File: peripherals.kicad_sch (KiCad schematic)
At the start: 93 parts, among them J10 533980471, J11 ERF8-040-05.0-L-DV-K-TR, J14 SM04B-SRSS-TB-LF-SN, J9 TC2050-IDC-NL, Q10 PJE138K, Q9 PJE138K, U30 TPD4E05U06QDQARQ1, U33 NTS0102GT, U34 PCAL6408ABSHP, U35 AP22653FDZ-7

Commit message: Renaming Sheets
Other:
- company: Antmicro Ltd -> Dronolab
- title: Jetson Orin Baseboard -> Peripherals
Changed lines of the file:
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@@
   (paper "A3")
   (title_block
-    (title "Jetson Orin Baseboard")
-    (date "2023-03-03")
-    (rev "1.1.0")
-    (company "Antmicro Ltd")
-    (comment 1 "www.antmicro.com")
+    (title "Peripherals")
+    (date "2023-07-05")
+    (rev "1.0.0")
+    (company "Dronolab")
+    (comment 1 "dronolab.etsmtl.ca")
   )
   (junction (at 248.285 253.365) (diameter 0) (color 0 0 0 0)

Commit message: Simplification continues
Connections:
- net DISABLE_POE_DCDC: no longer names the net of R25.4
- no-connect marks 12 -> 13

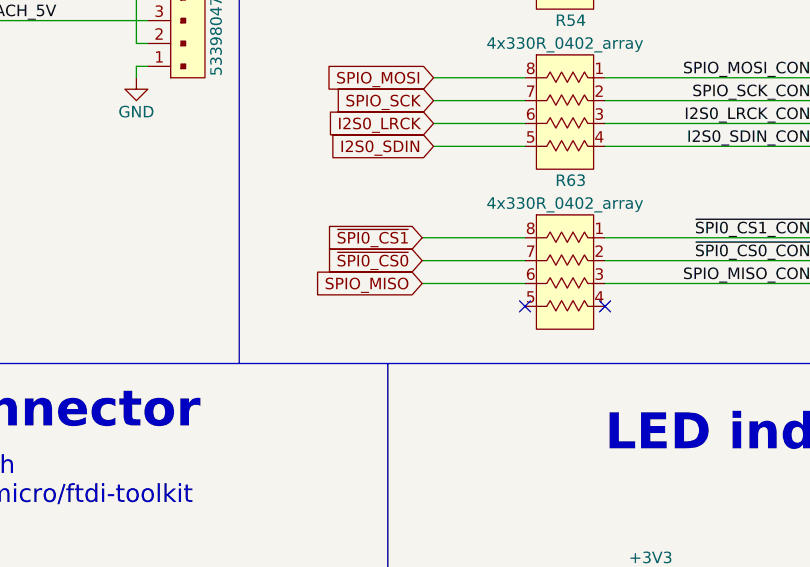
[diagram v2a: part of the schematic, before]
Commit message: Added IMU + MICROPHONES
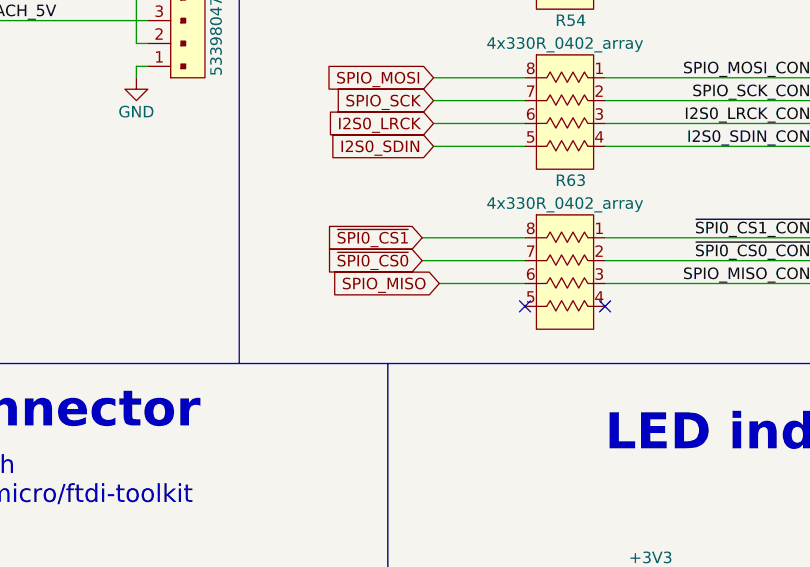
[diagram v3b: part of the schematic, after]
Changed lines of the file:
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@@
   (title_block
     (title "Peripherals")
-    (date "2023-07-05")
+    (date "2023-07-09")
     (rev "1.0.0")
     (company "Dronolab")
@@
     (stroke (width 0) (type default))
   )
-  (wire (pts (xy 110.49 196.85) (xy 121.92 196.85))
-    (stroke (width 0) (type default))
-  )
   (wire (pts (xy 224.79 144.78) (xy 198.12 144.78))
     (stroke (width 0) (type default))
@@
     (stroke (width 0) (type default))
   )
+  (wire (pts (xy 112.395 196.85) (xy 121.92 196.85))
+    (stroke (width 0) (type default))
+  )
   (wire (pts (xy 299.72 209.55) (xy 331.47 209.55))
     (stroke (width 0) (type default))
@@
     )
   )
-  (global_label "SPIO_MISO" (shape input) (at 110.49 196.85 180) (fields_autoplaced)
+  (global_label "SPIO_MISO" (shape input) (at 112.395 196.85 180) (fields_autoplaced)
     (effects (font (size 1.27 1.27)) (justify right))
-    (property "Intersheetrefs" "${INTERSHEET_REFS}" (at 98.0983 196.7706 0)
+    (property "Intersheetrefs" "${INTERSHEET_REFS}" (at 100.0033 196.7706 0)
       (effects (font (size 1.27 1.27)) (justify right))
     )

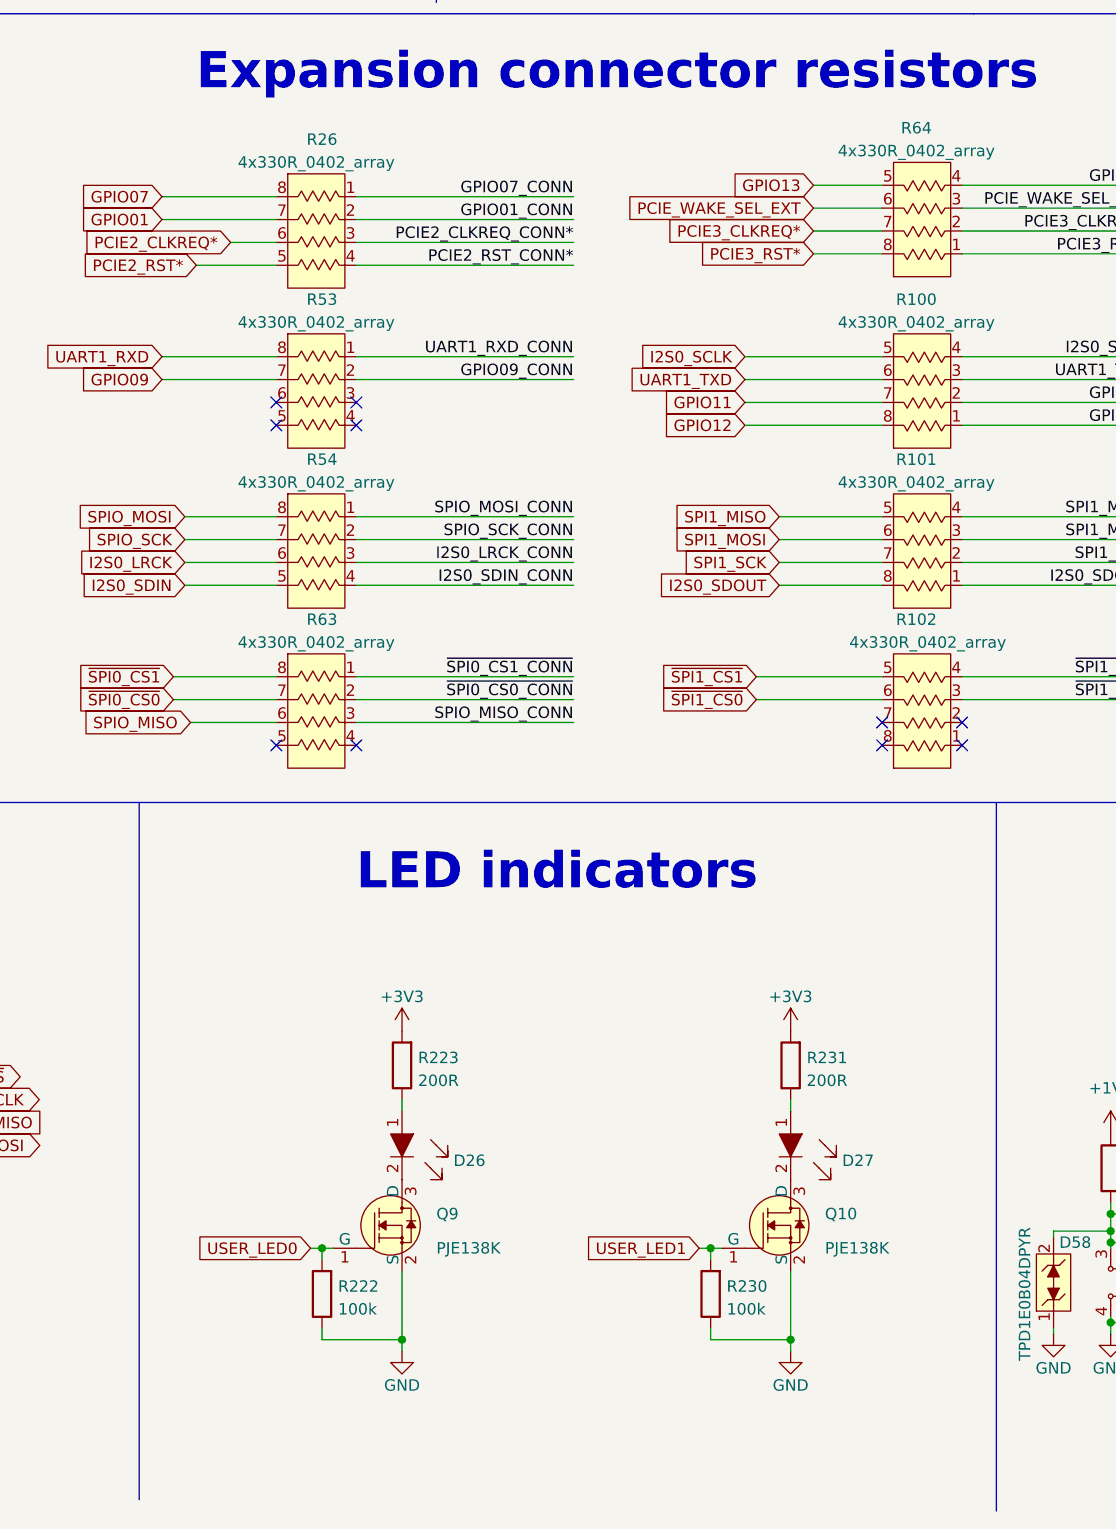
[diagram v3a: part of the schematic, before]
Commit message: Buzzer ajouté
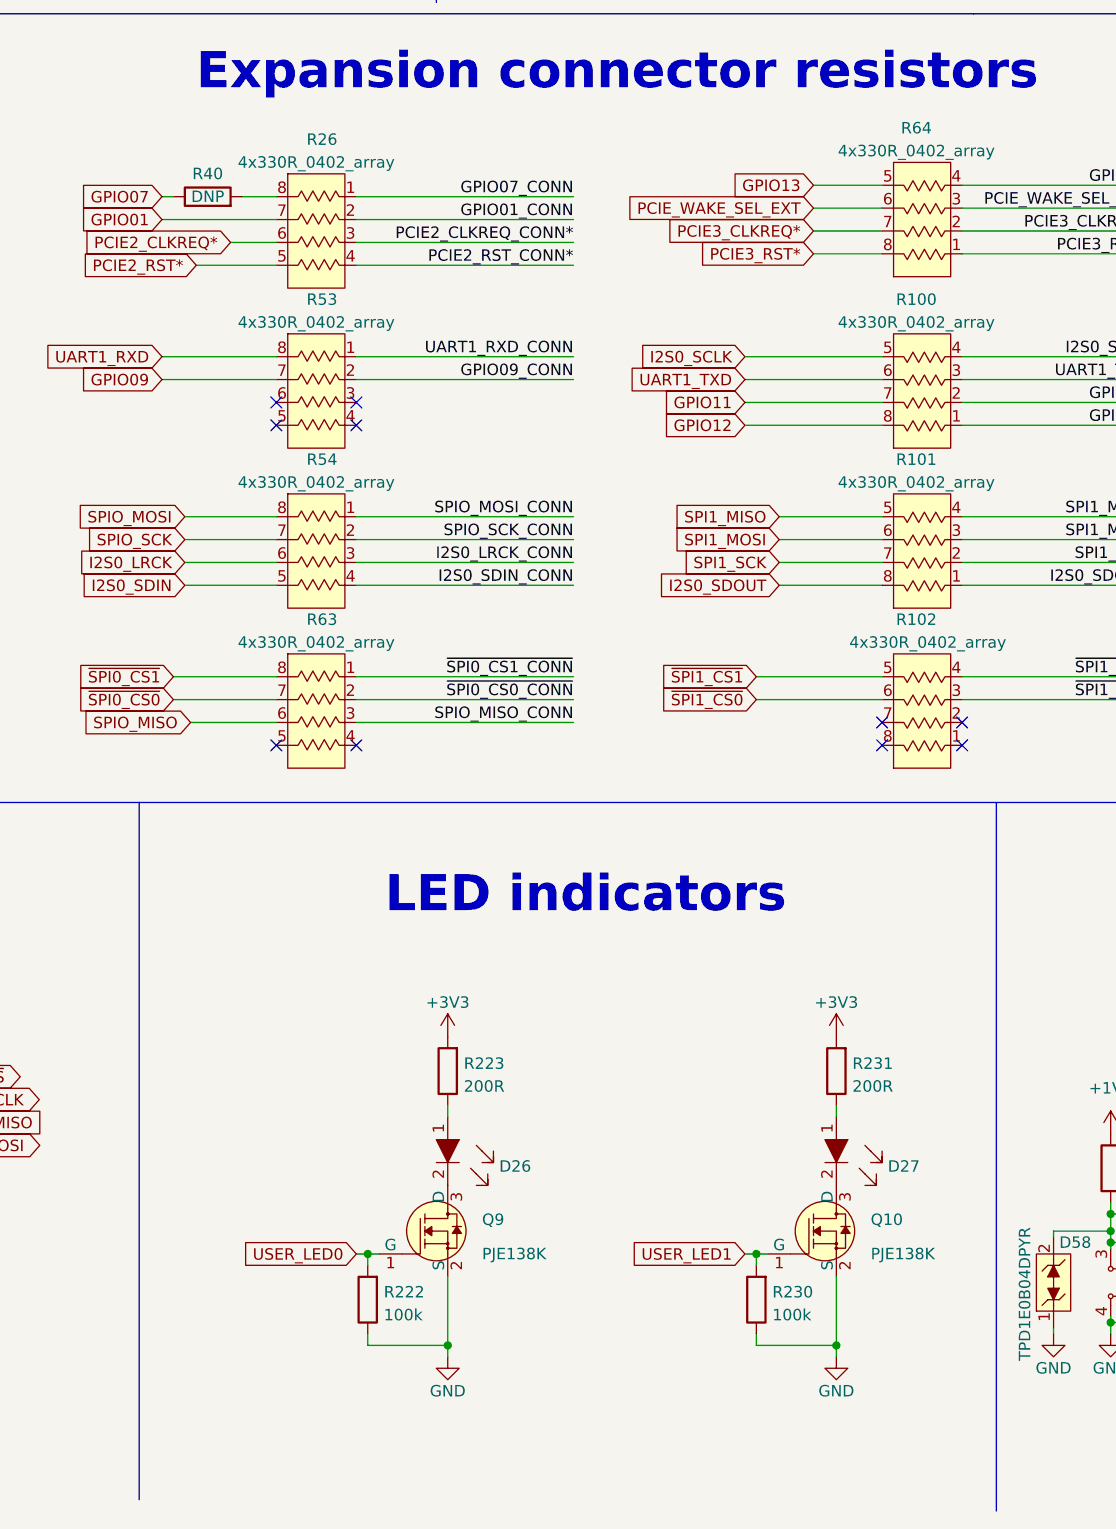
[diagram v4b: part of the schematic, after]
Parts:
- added R40: DNP, symbol Device:R
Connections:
- net GPIO07: now also R40.1; no longer R26.8
- new net: R26.8, R40.2
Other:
- moved on the sheet: D26, D27, Q10, Q9, R222, R223, R230, R231

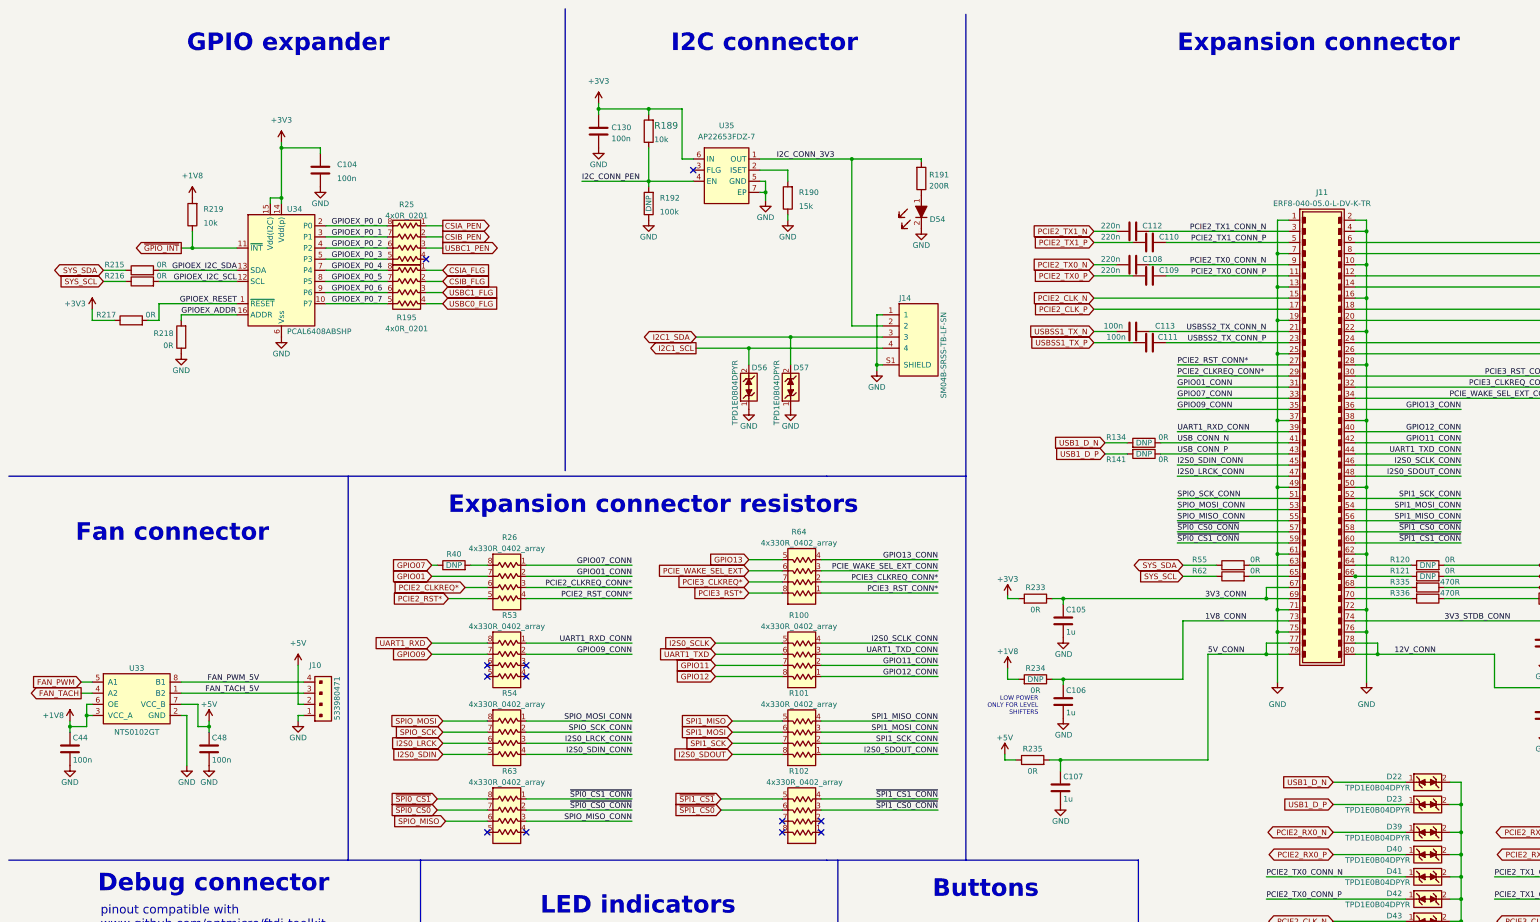
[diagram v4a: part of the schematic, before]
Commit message: Changes to CSI for multiplexing and to peripherals for better PAC connector
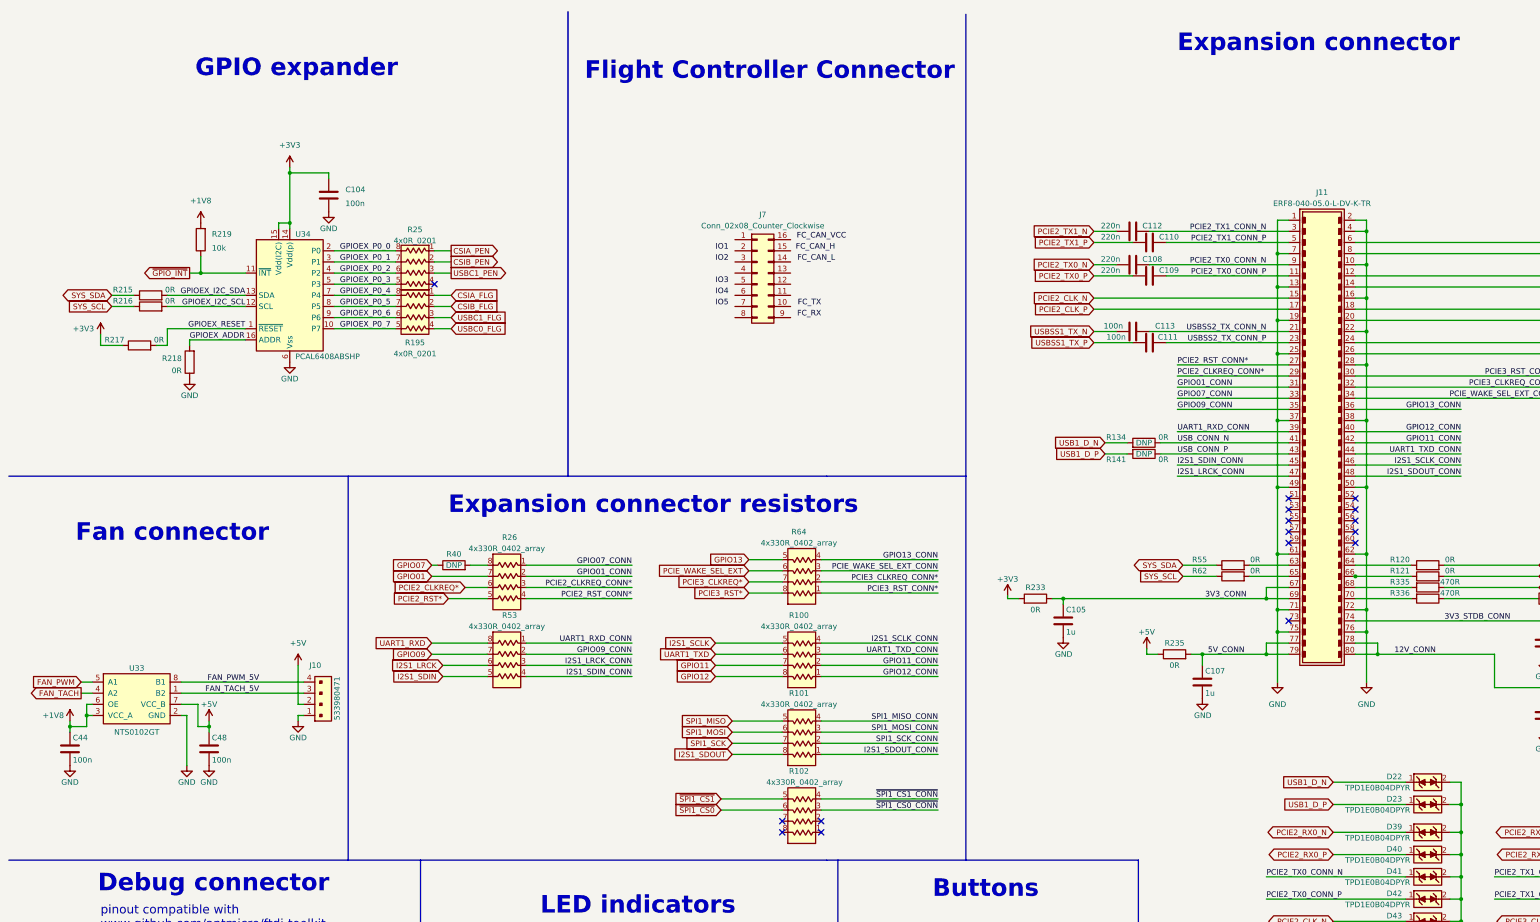
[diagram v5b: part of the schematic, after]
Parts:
- removed C106: C_1u_0402, jetson-orin-baseboard-footprints:0402-cap, symbol jetson-orin-baseboard:C_1u_0402
- removed C130: C_100n_0402, jetson-orin-baseboard-footprints:0402-cap, symbol jetson-orin-baseboard:C_100n_0402
- removed D54: LTST-C190GKT, jetson-orin-baseboard-footprints:LED_0603, symbol jetson-orin-baseboard:LTST-C190GKT
- removed D56, D57: TPD1E0B04DPYR, jetson-orin-baseboard-footprints:XDFN-2_1x0.60mm, symbol jetson-orin-baseboard:TPD1E0B04DPYR
- removed J14: SM04B-SRSS-TB-LF-SN, jetson-orin-baseboard-footprints:SM04B-SRSS-TB-LF-SN, symbol jetson-orin-baseboard:SM04B-SRSS-TB-LF-SN
- removed R189: R_10k_0402, jetson-orin-baseboard-footprints:0402-res, symbol jetson-orin-baseboard:R_10k_0402
- removed R190: R_15k_0402, jetson-orin-baseboard-footprints:0402-res, symbol jetson-orin-baseboard:R_15k_0402
- removed R191: R_200R_0402, jetson-orin-baseboard-footprints:0402-res, symbol jetson-orin-baseboard:R_200R_0402
- removed R192: R_100k_0402, jetson-orin-baseboard-footprints:0402-res, symbol jetson-orin-baseboard:R_100k_0402
- removed R234: R_0R_0603, jetson-orin-baseboard-footprints:0603-res, symbol jetson-orin-baseboard:R_0R_0603
- removed R54, R63: 4x330R_0402_array, jetson-orin-baseboard-footprints:R_Array_4x0402, symbol jetson-orin-baseboard:4x330R_0402_array
- removed U35: AP22653FDZ-7, jetson-orin-baseboard-footprints:DFN-6-1EP_2x2mm_P0.65mm_EP1x1.6mm, symbol jetson-orin-baseboard:AP22653FDZ-7
- added J7: Conn_02x08_Counter_Clockwise, symbol Connector_Generic:Conn_02x08_Counter_Clockwise
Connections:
- net I2S0_LRCK_CONN is gone; now on net I2S1_LRCK_CONN: J11.47
- net I2S0_SDIN_CONN is gone; now on net I2S1_SDIN_CONN: J11.45
- net SPI1_MISO_CONN: no longer J11.56
- net SPI1_MOSI_CONN: no longer J11.54
- net SPI1_SCK_CONN: no longer J11.52
- net ~{SPI1_CS0_CONN}: no longer J11.58
- net ~{SPI1_CS1_CONN}: no longer J11.60
- net I2S1_LRCK_CONN: now reaches R53.3
- net I2S1_SDIN_CONN: now reaches R53.4
- net I2S1_SDIN: now reaches R53.5
- net I2S1_LRCK: now reaches R53.6
- net 1V8_CONN: no longer names the net of J11.73
- net I2S0_SCLK renamed I2S1_SCLK
- net I2S0_SCLK_CONN renamed I2S1_SCLK_CONN
- net I2S0_SDOUT renamed I2S1_SDOUT
- net I2S0_SDOUT_CONN renamed I2S1_SDOUT_CONN
- net SPIO_MISO_CONN: no longer names the net of J11.55
- net SPIO_MOSI_CONN: no longer names the net of J11.53
- net SPIO_SCK_CONN: no longer names the net of J11.51
- net ~{SPI0_CS0_CONN}: no longer names the net of J11.57
- net ~{SPI0_CS1_CONN}: no longer names the net of J11.59
- no-connect marks 13 -> 17
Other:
- note added: "Flight Controller Connector"
- note removed: "I2C connector"
- note removed: "LOW POWER ONLY FOR LEVEL SHIFTERS"
- moved on the sheet: C104, C107, R195, R215, R216, R217, R218, R219, R235, R25, U34

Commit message: little changes that day
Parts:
- removed C114: C_1u_0402, jetson-orin-baseboard-footprints:0402-cap, symbol jetson-orin-baseboard:C_1u_0402
- removed R247: R_0R_0603, jetson-orin-baseboard-footprints:0603-res, symbol jetson-orin-baseboard:R_0R_0603
- added C94: C_1u_0402, jetson-orin-baseboard-footprints:0402-cap, symbol jetson-orin-baseboard:C_1u_0402
- added R54: R_0R_0603, jetson-orin-baseboard-footprints:0603-res, symbol jetson-orin-baseboard:R_0R_0603
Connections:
- net 3V3_STDB: now also R54.2
- net 3V3_STDB_CONN: now also J11.73, C94.1, R54.1; no longer J11.74
- net FC_CAN_H: now also J11.54, J7.15 (Pin_15)
- net FC_CAN_L: now also J11.56, J7.14 (Pin_14)
- net FC_RX: now also J11.62, J7.10 (Pin_10)
- net FC_TX: now also J11.64, J7.11 (Pin_11)
- net GND: now also J11.60, J11.66, J7.1 (Pin_1), J7.12 (Pin_12), J7.4 (Pin_4), J7.8 (Pin_8), J7.9 (Pin_9), C94.2; no longer J11.10, J11.16, J11.2, J11.22, J11.28, J11.38, J11.4, J11.50, J11.62, J11.72
- net IO1: now also J11.51, J7.2 (Pin_2)
- net IO2: now also J11.53, J7.3 (Pin_3)
- net IO3: now also J11.55, J7.5 (Pin_5)
- net IO4: now also J11.57, J7.6 (Pin_6)
- net IO5: now also J11.59, J7.7 (Pin_7)
- net GND1: now reaches J7.13 (Pin_13)
- net GND1: now also J11.52, J11.58, J7.16 (Pin_16)
- net at R336.2: now also J11.74; no longer J11.70
- net at R121.1: now also J11.70; no longer J11.66
- net at R335.2: now also J11.72; no longer J11.68
- net at R120.1: now also J11.68; no longer J11.64
- new net: J11.10, J11.16, J11.2, J11.22, J11.28, J11.38, J11.4, J11.50
- no-connect marks 17 -> 6
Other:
- moved on the sheet: C105, R120, R121, R233, R335, R336
